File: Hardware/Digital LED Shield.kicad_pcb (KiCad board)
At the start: 2 copper layers, 22 x 26.5 mm, 18 parts, among them IC1 TPS2420RSAT, IC2 LM66200DRLR, J1 Conn_02x10_Odd_Even, J2 Conn_01x03_Male, J3 Barrel_Jack_MountingPin, J4 Conn_01x02_Female, J5 Conn_01x03_Male, U1 SN74LVC1T45DBV

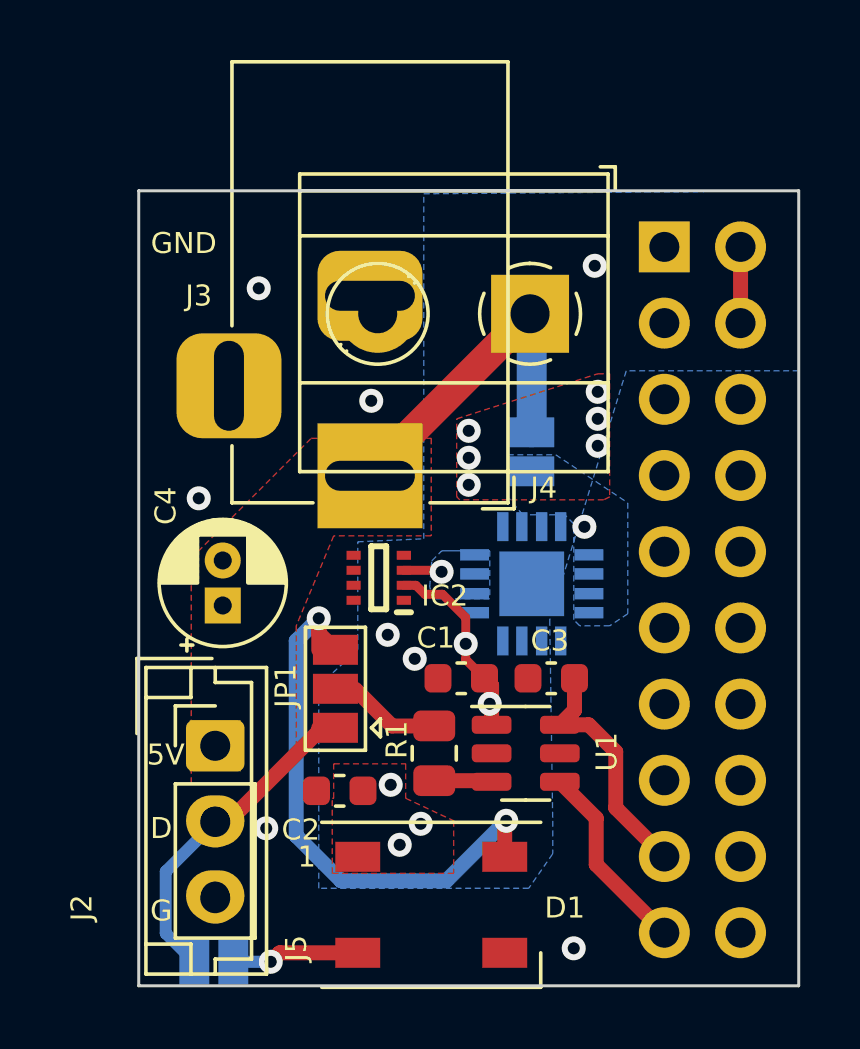
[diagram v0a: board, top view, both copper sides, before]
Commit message: add eFuse for Overvoltage and Overcurrent protection
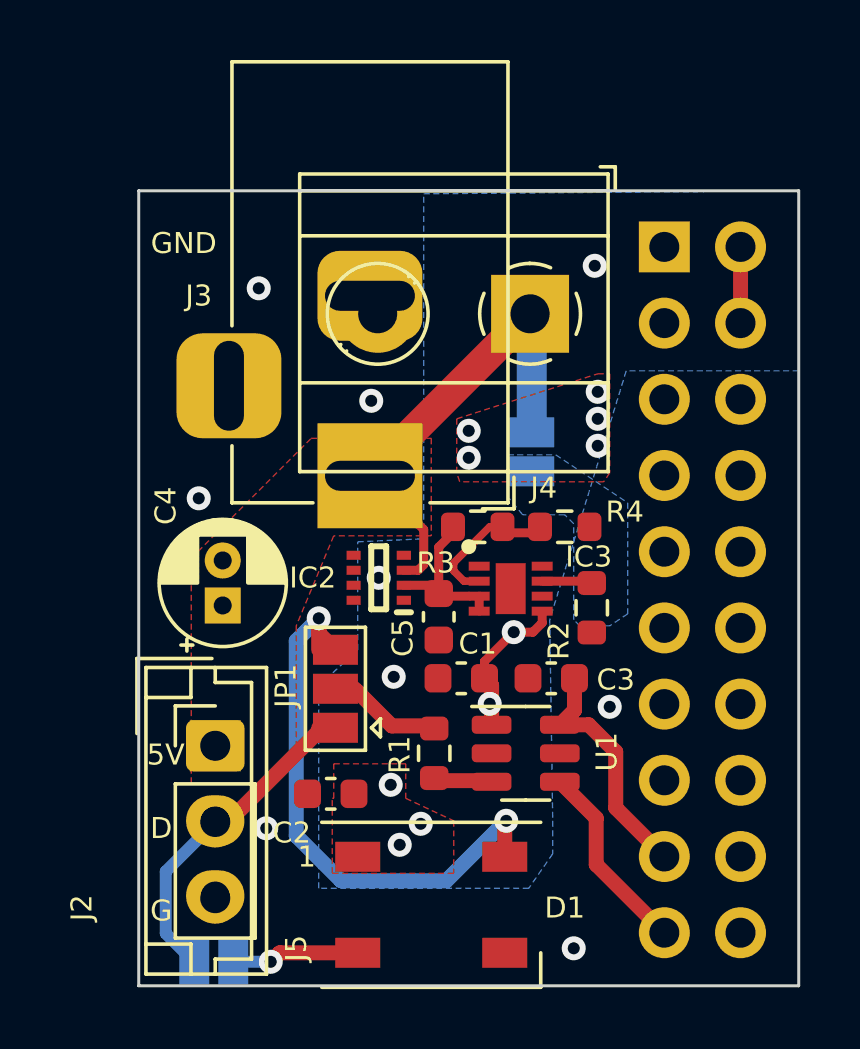
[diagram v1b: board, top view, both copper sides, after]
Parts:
- removed IC1: TPS2420RSAT, TPS2420RSAT:QFN65P400X400X100-17N
- added C5: 0.1uF, Capacitor_SMD:C_0603_1608Metric, F.Cu at (134.0, 97.7)
- added IC3: TPS259570DSGR, TPS2595:SON50P200X200X80-9N, F.Cu at (136.4, 96.8)
- added R2: 953, Resistor_SMD:R_0603_1608Metric, F.Cu at (139.1, 97.4)
- added R3: 1k, Resistor_SMD:R_0603_1608Metric, F.Cu at (135.3, 94.7)
- added R4: 296,3k, Resistor_SMD:R_0603_1608Metric, F.Cu at (138.2, 94.7)
- R1: footprint Resistor_SMD:R_0805_2012Metric -> Resistor_SMD:R_0603_1608Metric
- moved C2 0.32 mm to (130.4, 103.6)
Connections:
- IC2 pad 2: +5VP -> +5VL
- IC2 pad 3: +5VL -> +5V
- JP2 pad 2: +5VD -> +5VP
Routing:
- net Net-(IC3-Pad2): track 0.00 -> 4.64 mm
- net +5V: track 11.6 -> 16.0 mm
- net +5VL: track 1.28 -> 4.86 mm, vias 1 -> 0
- net Net-(IC3-Pad7): track 0.00 -> 1.85 mm
- net +5VP: track 8.98 -> 7.46 mm, vias 12 -> 10
- net GND: vias 8 -> 9
- removed copper zone on B.Cu, net +5VD
- removed copper zone on B.Cu, net +5VL
